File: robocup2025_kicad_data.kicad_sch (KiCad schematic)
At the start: 8 parts, among them U1 RASPBERRY_PI_4B_4GB, U2 ESP32-DEVKITC-32E

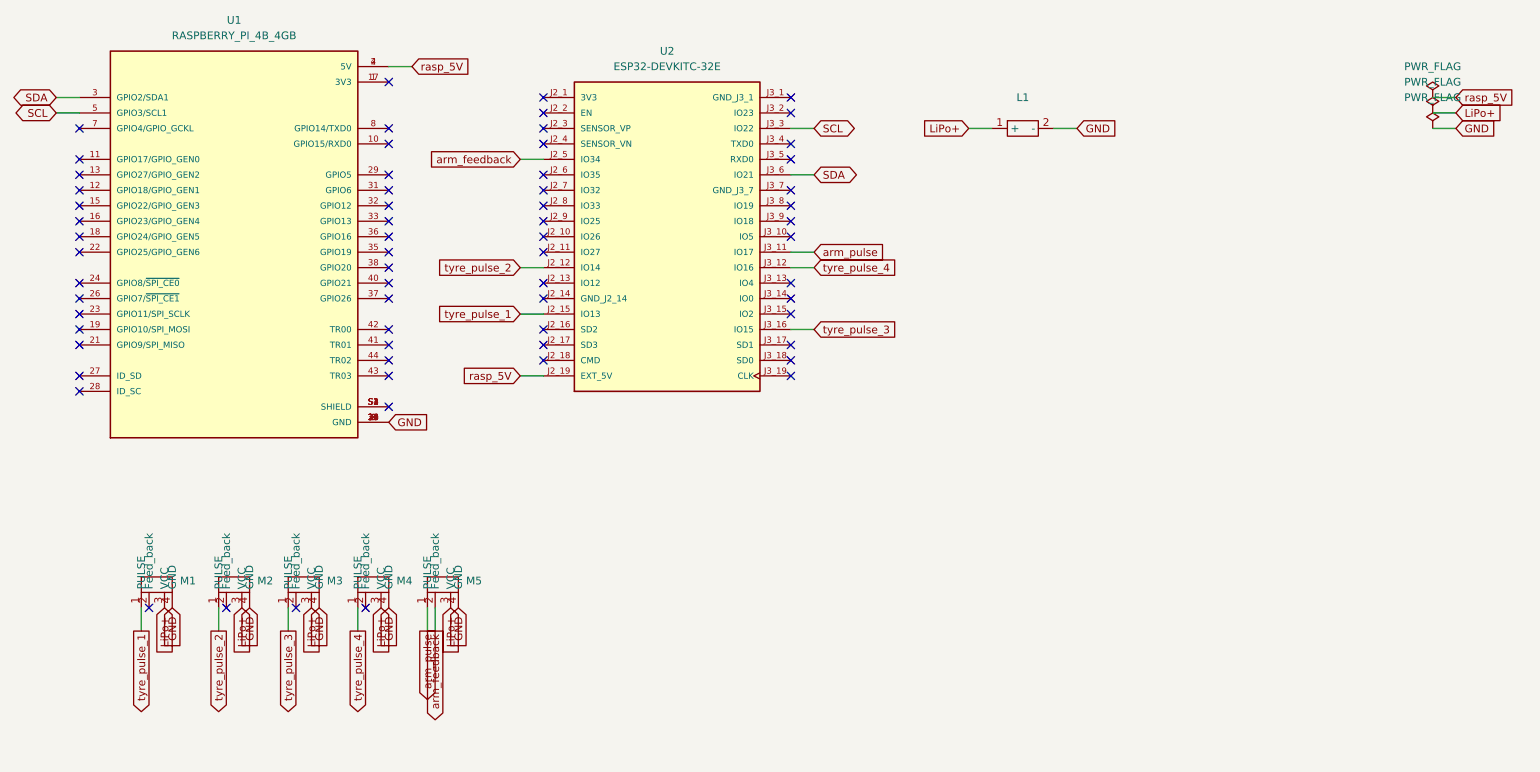
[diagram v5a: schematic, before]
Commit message: robocup2025_kicad_data.kicad_sch: Connected ultrasonic sensor
ERC passing
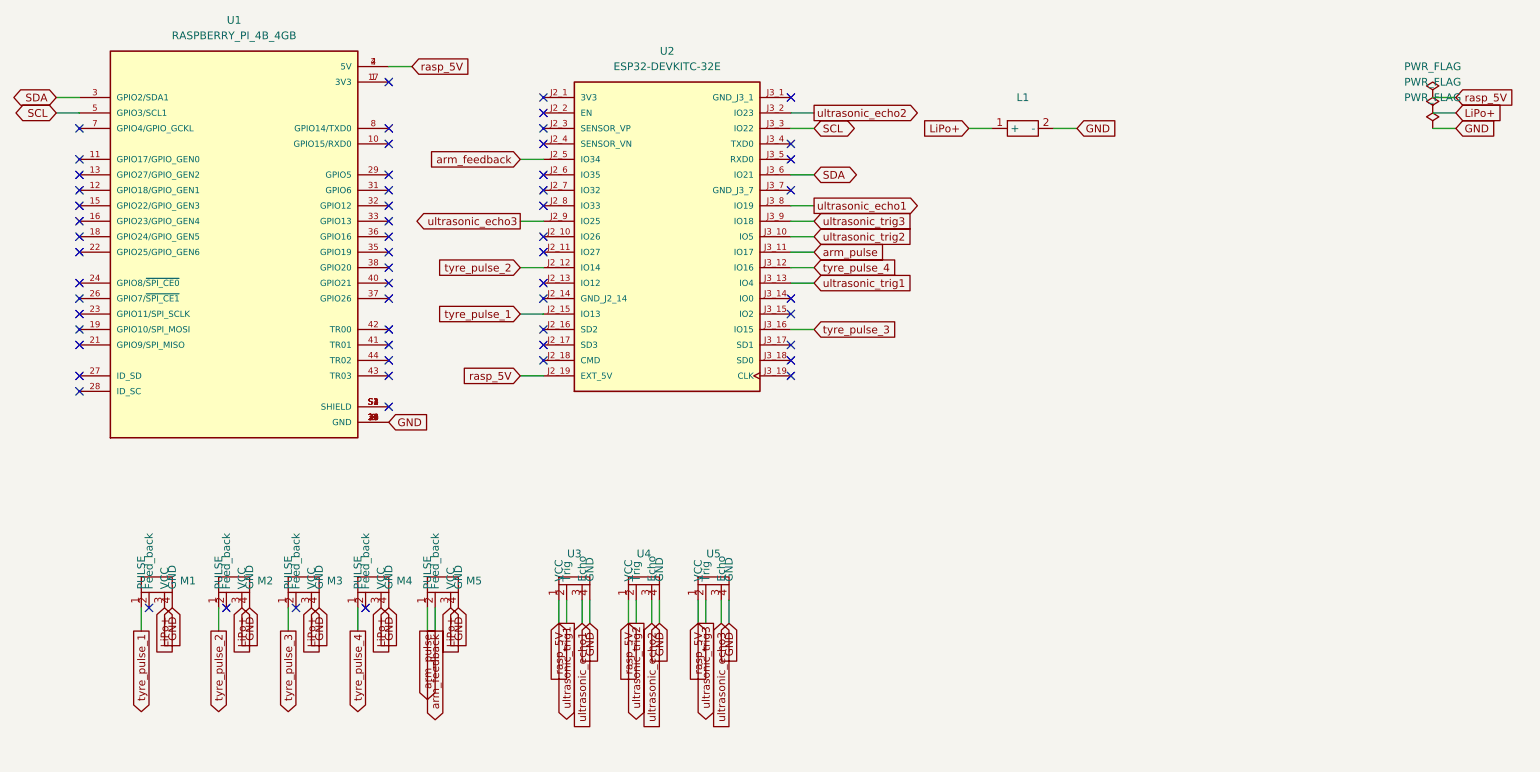
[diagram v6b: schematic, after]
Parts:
- added U3, U4, U5: ~, symbol robo:ultrasonic_sensor
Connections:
- net GND: now also U3.4 (GND), U4.4 (GND), U5.4 (GND)
- net rasp_5V: now also U3.1 (VCC), U4.1 (VCC), U5.1 (VCC)
- net ultrasonic_echo3: now reaches U2.J2_9 (IO25)
- net ultrasonic_echo3: now also U5.3 (Echo)
- net ultrasonic_trig2: now reaches U2.J3_10 (IO5)
- net ultrasonic_trig2: now also U4.2 (Trig)
- net ultrasonic_trig1: now reaches U2.J3_13 (IO4)
- net ultrasonic_trig1: now also U3.2 (Trig)
- net ultrasonic_echo2: now reaches U2.J3_2 (IO23)
- net ultrasonic_echo2: now also U4.3 (Echo)
- net ultrasonic_echo1: now reaches U2.J3_8 (IO19)
- net ultrasonic_echo1: now also U3.3 (Echo)
- net ultrasonic_trig3: now reaches U2.J3_9 (IO18)
- net ultrasonic_trig3: now also U5.2 (Trig)
- no-connect marks 65 -> 59

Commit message: robocup2025_kicad_data.kicad_sch: Added footprint for sch
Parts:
- L1: footprint (none) -> robo:LiPo
- M1, M2, M3, M4, M5: footprint (none) -> robo:servo_motor
- U1: footprint RASPBERRY_PI_4B_4GB:MODULE_RASPBERRY_PI_4B_4GB -> robo:MODULE_RASPBERRY_PI_4B_4GB
- U2: footprint ESP32-DEVKITC-32E:MODULE_ESP32-DEVKITC-32E -> robo:MODULE_ESP32-DEVKITC-32E
- U3, U4, U5: footprint (none) -> robo:ultrasonic
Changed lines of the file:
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@@
 			)
 		)
-		(property "Footprint" "RASPBERRY_PI_4B_4GB:MODULE_RASPBERRY_PI_4B_4GB"
+		(property "Footprint" "robo:MODULE_RASPBERRY_PI_4B_4GB"
 			(at 54.61 63.5 0)
 			(effects
@@
 			)
 		)
-		(property "Footprint" ""
+		(property "Footprint" "robo:ultrasonic"
 			(at 133.35 118.11 0)
 			(effects
@@
 			)
 		)
-		(property "Footprint" ""
+		(property "Footprint" "robo:servo_motor"
 			(at 54.61 118.11 0)
 			(effects
@@
 			)
 		)
-		(property "Footprint" ""
+		(property "Footprint" "robo:LiPo"
 			(at 184.15 43.18 0)
 			(effects
@@
 			)
 		)
-		(property "Footprint" "ESP32-DEVKITC-32E:MODULE_ESP32-DEVKITC-32E"
+		(property "Footprint" "robo:MODULE_ESP32-DEVKITC-32E"
 			(at 125.73 60.96 0)
 			(effects
@@
 			)
 		)
-		(property "Footprint" ""
+		(property "Footprint" "robo:servo_motor"
 			(at 66.04 118.11 0)
 			(effects
@@
 			)
 		)
-		(property "Footprint" ""
+		(property "Footprint" "robo:ultrasonic"
 			(at 110.49 118.11 0)
 			(effects
@@
 			)
 		)
-		(property "Footprint" ""
+		(property "Footprint" "robo:servo_motor"
 			(at 77.47 118.11 0)
 			(effects
@@
 			)
 		)
-		(property "Footprint" ""
+		(property "Footprint" "robo:servo_motor"
 			(at 88.9 118.11 0)
 			(effects
@@
 			)
 		)
-		(property "Footprint" ""
+		(property "Footprint" "robo:servo_motor"
 			(at 41.91 118.11 0)
 			(effects
@@
 			)
 		)
-		(property "Footprint" ""
+		(property "Footprint" "robo:ultrasonic"
 			(at 121.92 118.11 0)
 			(effects

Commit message: robocup2025_kicad_data.kicad_pcb,robocup2025_kicad_data.kicad_sch: Commit
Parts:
- U1: footprint robo:MODULE_RASPBERRY_PI_4B_4GB -> robo:raspberrypi5 small
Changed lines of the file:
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@@
 			)
 		)
-		(property "Footprint" "robo:MODULE_RASPBERRY_PI_4B_4GB"
+		(property "Footprint" "robo:raspberrypi5 small"
 			(at 54.61 63.5 0)
 			(effects
